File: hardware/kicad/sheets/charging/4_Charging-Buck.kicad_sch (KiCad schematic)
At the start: 38 parts, among them Q3 L2N7002SLLT1G, Q4 ME50P06-G, U7 68uF, U8 CN3722, U9 15uH

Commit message: various improvements
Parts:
- renumbered C5 to C12, C6 to C13, C7 to C14, C8 to C15, C9 to C16, C10 to C17, C11 to C18, C12 to C19, C13 to C20, C14 to C21, C15 to C22, C16 to C23, C17 to C24, D10 to D13, D11 to D14, R6 to R15, R7 to R16, R8 to R17, R9 to R18, R10 to R19, R11 to R20, R12 to R21, R13 to R22, R14 to R23, R15 to R24, R16 to R25, R17 to R26, R18 to R27, R19 to R28, R20 to R29, R21 to R30

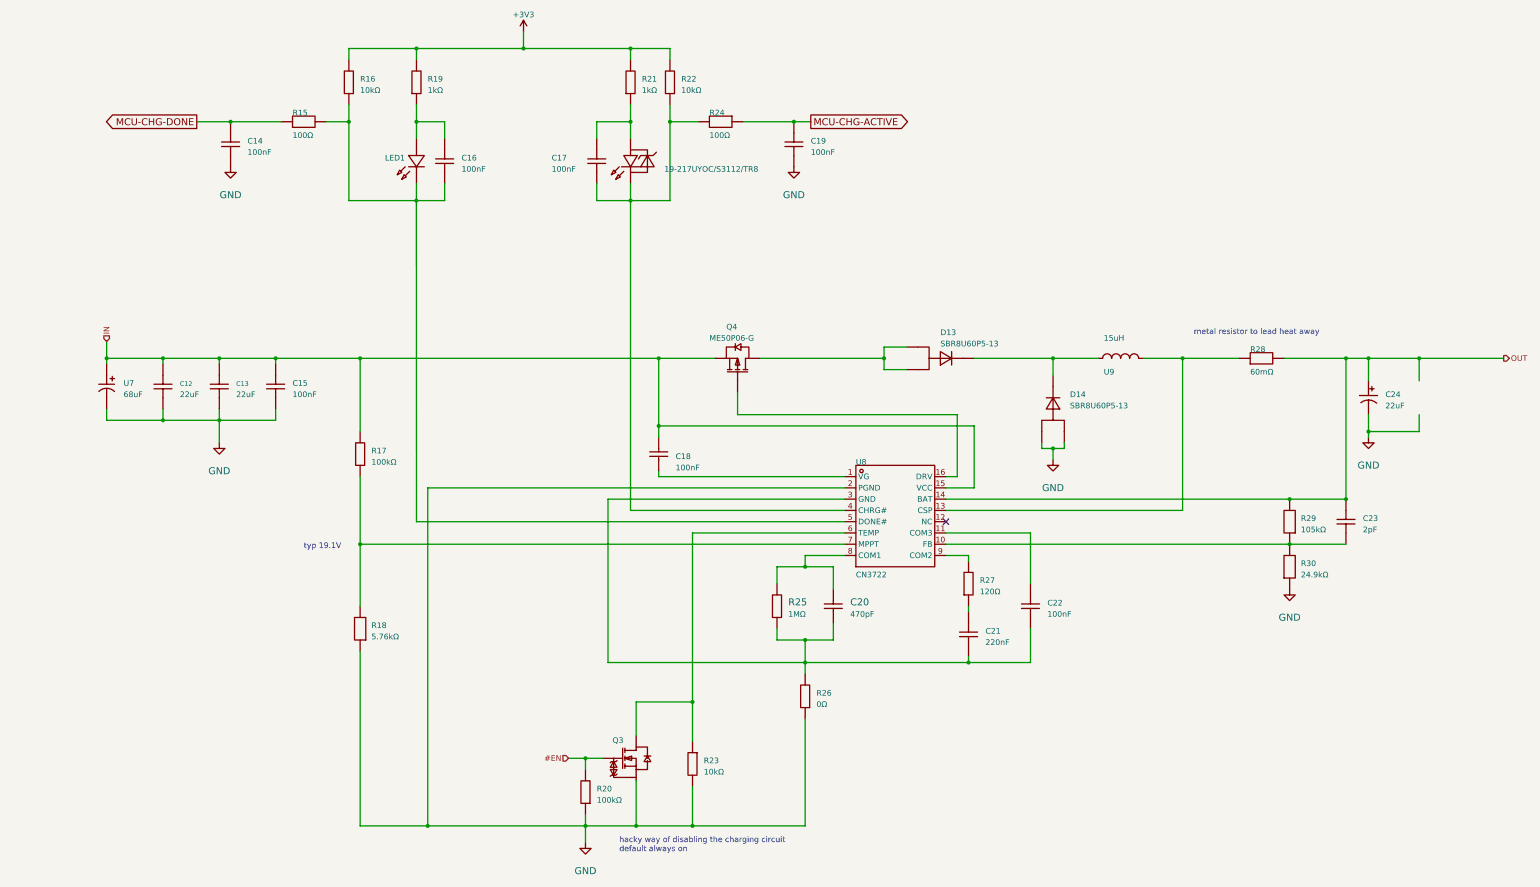
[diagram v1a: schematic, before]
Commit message: current sensing on the servos and cleaning up empty sheets
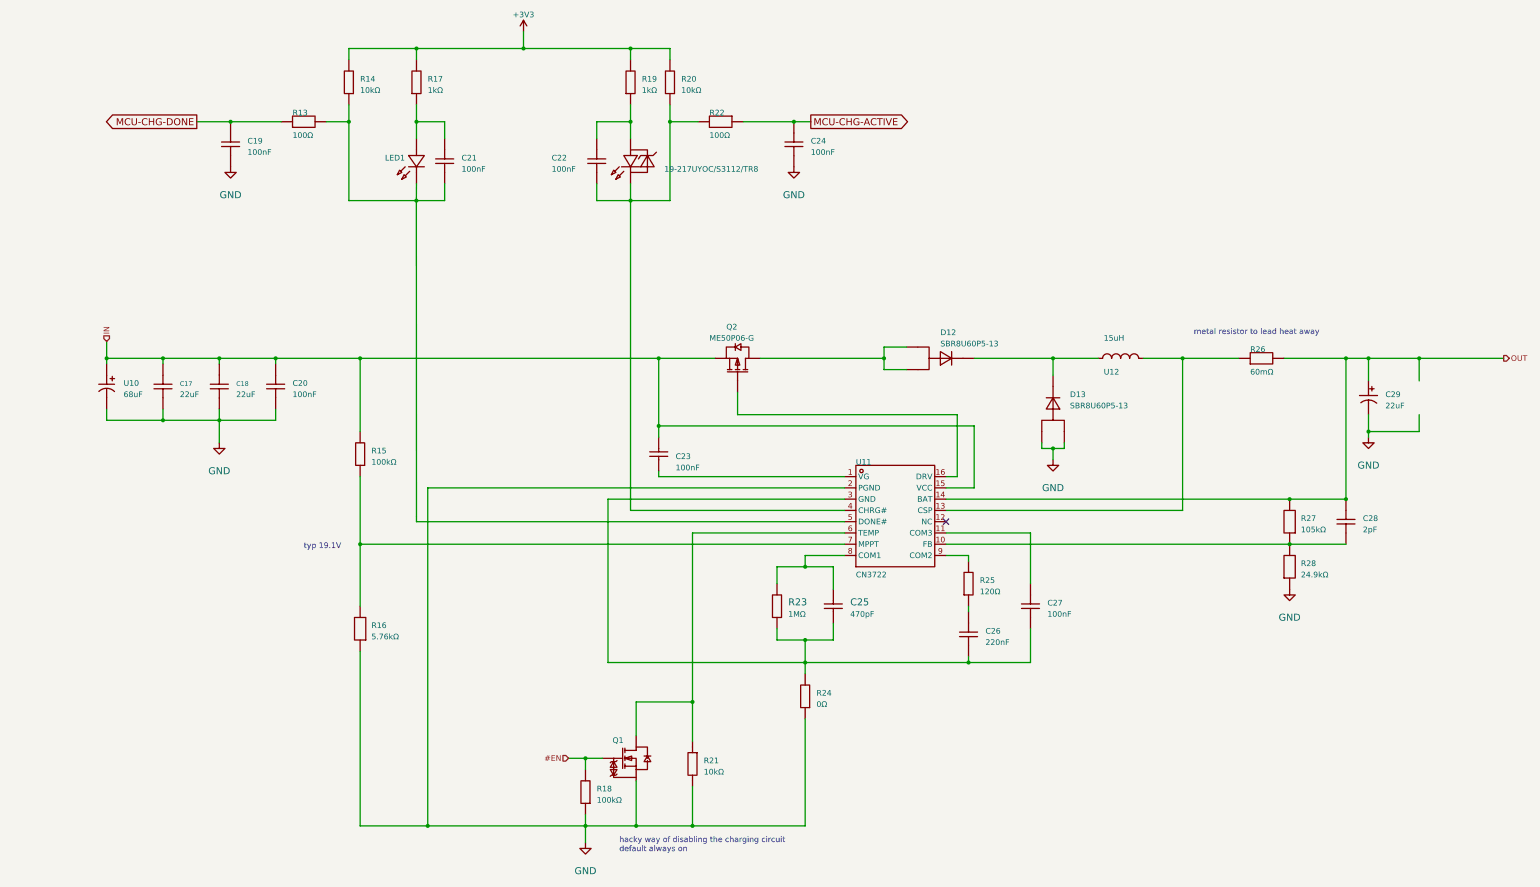
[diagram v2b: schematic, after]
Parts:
- renumbered C12 to C17, C13 to C18, C14 to C19, C15 to C20, C16 to C21, C17 to C22, C18 to C23, C19 to C24, C20 to C25, C21 to C26, C22 to C27, C23 to C28, C24 to C29, D13 to D12, D14 to D13, Q3 to Q1, Q4 to Q2, R15 to R13, R16 to R14, R17 to R15, R18 to R16, R19 to R17, R20 to R18, R21 to R19, R22 to R20, R23 to R21, R24 to R22, R25 to R23, R26 to R24, R27 to R25, R28 to R26, R29 to R27, R30 to R28, U7 to U10, U8 to U11, U9 to U12

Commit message: new references
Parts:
- renumbered C17 to C18, C18 to C19, C19 to C20, C20 to C21, C21 to C22, C22 to C23, C23 to C24, C24 to C25, C25 to C26, C26 to C27, C27 to C28, C28 to C29, C29 to C30, D12 to D11, D13 to D12, LED1 to LED6, LED2 to LED7, R13 to R35, R14 to R36, R15 to R37, R16 to R38, R17 to R39, R18 to R40, R19 to R41, R20 to R42, R21 to R43, R22 to R44, R23 to R45, R24 to R46, R25 to R47, R26 to R48, R27 to R49, R28 to R50, U10 to U15, U11 to U16, U12 to U17

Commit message: pre robot updating references
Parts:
- renumbered C18 to C17, C19 to C18, C20 to C19, C21 to C20, C22 to C21, C23 to C22, C24 to C23, C25 to C24, C26 to C25, C27 to C26, C28 to C27, C29 to C28, C30 to C29, R35 to R43, R36 to R44, R37 to R45, R38 to R46, R39 to R47, R40 to R48, R41 to R49, R42 to R50, R43 to R51, R44 to R52, R45 to R53, R46 to R54, R47 to R55, R48 to R56, R49 to R57, R50 to R58, U15 to U16, U16 to U17, U17 to U18

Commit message: various imprvements
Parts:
- added R196: --, symbol 5v rail sm-easyedapro:PE2512FKE7W0R06L
- renumbered C17 to C22, C18 to C23, C19 to C24, C20 to C25, C21 to C26, C22 to C27, C23 to C28, C24 to C29, C25 to C30, C26 to C31, C27 to C32, C28 to C33, C29 to C34, R43 to R73, R44 to R74, R45 to R75, R46 to R76, R47 to R77, R48 to R78, R49 to R79, R50 to R80, R51 to R81, R52 to R82, R53 to R83, R54 to R84, R55 to R85, R56 to R86, R57 to R87, R58 to R88, U16 to U22, U17 to U23, U18 to U24
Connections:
- net MCU-CHG-ACTIVE is gone; now on net Charger/CN3072/CHG-ACTIVE: C29.2, R82.1
- net MCU-CHG-DONE is gone; now on net Charger/CN3072/CHG-DONE: C24.2, R73.1
- net OUT: now also R196.2
- net at R86.1, U23.13 (CSP), U24.2: now also R196.1
- net Charger/CN3072/CHG-DONE: now reaches C27.1, LED7.1 (-), R80.1, R82.2, U23.4 (CHRG#)
- net Charger/CN3072/CHG-ACTIVE: now reaches C26.1, LED6.1 (K), R73.2, R74.1, U23.5 (DONE#)
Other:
- note added: "Default 3A, solder another in parallel for higher current"

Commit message: updated some footprints, fixed board
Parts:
- removed C34: 22uF, symbol 5v rail sm-easyedapro:RVT1H220M0605
- removed Q1: L2N7002SLLT1G, symbol 5v rail sm-easyedapro:L2N7002SLLT1G
- removed R73, R82: 100Ω, symbol 5v rail sm-easyedapro:FRC0402F1000TS
- removed R74, R80: 10kΩ, symbol 5v rail sm-easyedapro:0402WGF1002TCE
- removed U22: 68uF, symbol 5v rail sm-easyedapro:RVT1H680M0607
- added C135: RVT1H220M0605, JLCImport:RVT1H220M0605, symbol JLCImport:RVT1H220M0605
- added Q19: L2N7002SLLT1G, JLCImport:L2N7002SLLT1G, symbol JLCImport:L2N7002SLLT1G
- added R109, R73: 0603WAF1000T5E, JLCImport:0603WAF1000T5E, symbol JLCImport:0603WAF1000T5E
- added R74, R82: 10k, Resistor_SMD:R_0201_0603Metric, symbol Device:R
- added U69: RVT1H680M0607, JLCImport:RVT1H680M0607, symbol JLCImport:RVT1H680M0607
- C20: renamed from C22; footprint (none) -> 5v rail sm-easyedapro:C0805; now in the parts list
- C21: renamed from C23; footprint (none) -> 5v rail sm-easyedapro:C0805; now in the parts list
- C22: renamed from C24; footprint (none) -> 5v rail sm-easyedapro:C0402; now in the parts list
- C23: renamed from C25; footprint (none) -> 5v rail sm-easyedapro:C0402; now in the parts list
- C24: renamed from C26; footprint (none) -> 5v rail sm-easyedapro:C0402; now in the parts list
- C25: renamed from C27; footprint (none) -> 5v rail sm-easyedapro:C0402; now in the parts list
- C26: renamed from C28; footprint (none) -> 5v rail sm-easyedapro:C0402; now in the parts list
- C27: renamed from C29; footprint (none) -> 5v rail sm-easyedapro:C0402; now in the parts list
- C29: renamed from C31; footprint (none) -> 5v rail sm-easyedapro:C0603; now in the parts list
- C30: renamed from C32; footprint (none) -> 5v rail sm-easyedapro:C0402; now in the parts list
- C31: renamed from C33; footprint (none) -> 5v rail sm-easyedapro:C0402; now in the parts list
- D11: footprint (none) -> JLCImport:SBR8U60P5-13; now in the parts list
- D12: footprint 5v rail sm-easyedapro:POWERDI-5_L5.4-W4.0-LS6.5-RD -> JLCImport:SBR8U60P5-13
- LED6: footprint (none) -> JLCImport:PSC-1608U50GC-G4; Silkscreen (none) -> 100%; now in the parts list
- LED7: footprint (none) -> JLCImport:19-217UYOC_S3112_TR8; Silkscreen text (none) -> Charging; now in the parts list
- Q2: footprint (none) -> Package_TO_SOT_SMD:TO-252-2; now in the parts list
- R76, R77, R78, R81, R83, R85: footprint (none) -> Resistor_SMD:R_0603_1608Metric; now in the parts list
- R86: footprint (none) -> JLCImport:PE2512FKE7W0R06L; now in the parts list
- R87: renamed from R196; footprint (none) -> JLCImport:PE2512FKE7W0R06L; now not fitted
- R89: renamed from R88; footprint (none) -> Resistor_SMD:R_0603_1608Metric; now in the parts list
- U23: renamed from U24; now in the parts list
- renumbered C30 to C28, R87 to R88, U23 to U22
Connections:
- net #EN: now also Q19.1 (G)
- net +3V3: now also R74.1, R82.1
- net Charger/CN3072/CHG-ACTIVE: now also R109.2, R73.2, R74.2
- net Charger/CN3072/CHG-DONE: now also R109.1, R73.1, R82.2
- net GND: now also C135.2, Q19.2 (S)
- net OUT: now also C135.1
- net at R81.1, U22.6 (TEMP): now also Q19.3 (D)
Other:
- moved on the sheet: R78

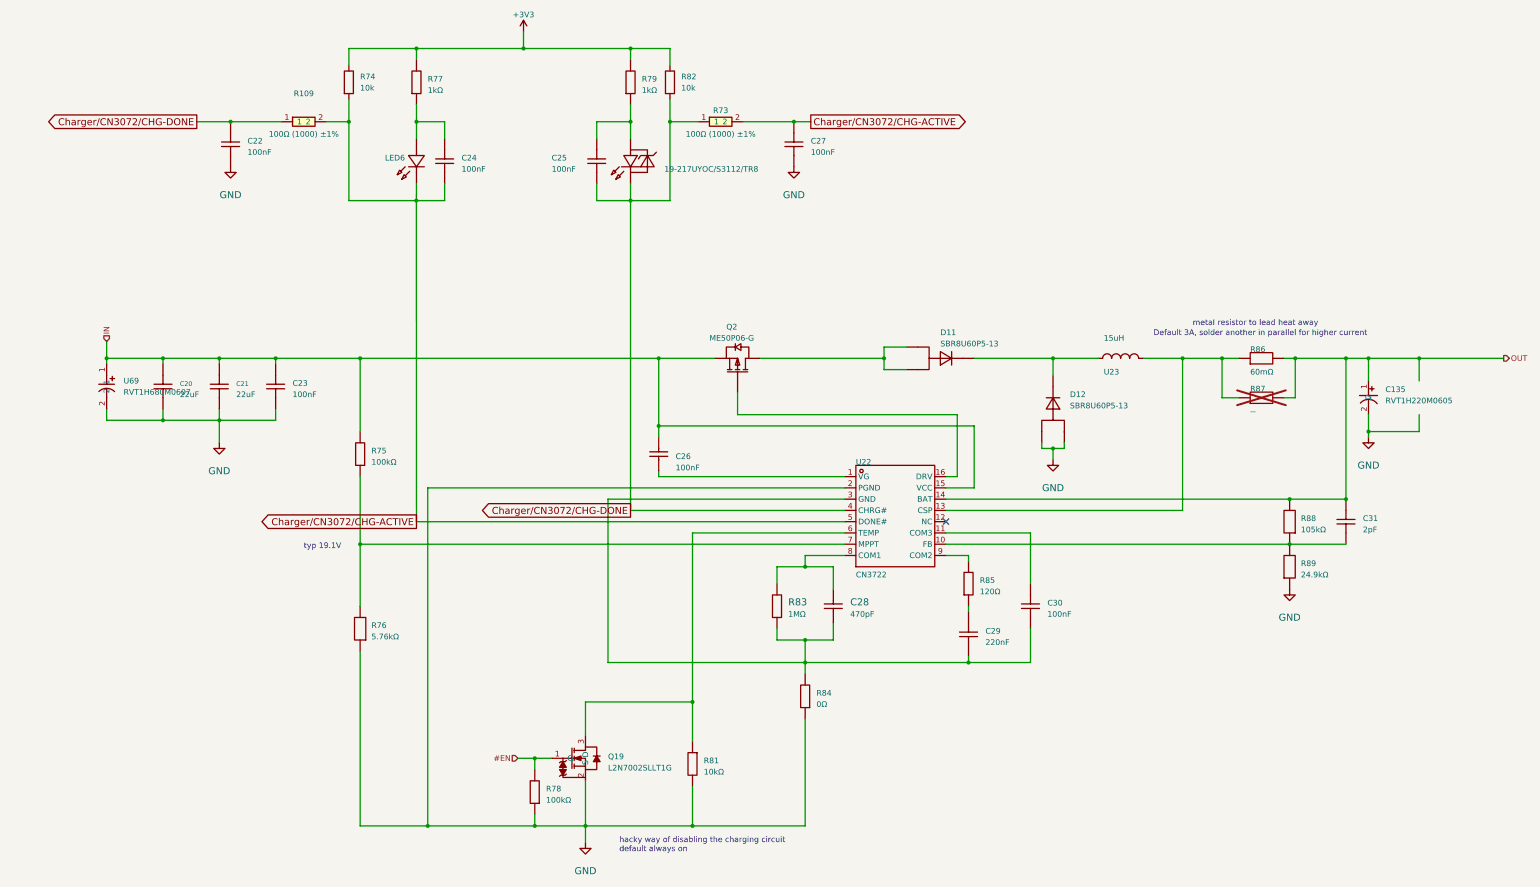
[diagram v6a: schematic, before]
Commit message: 5v usb c done, esc mostly done
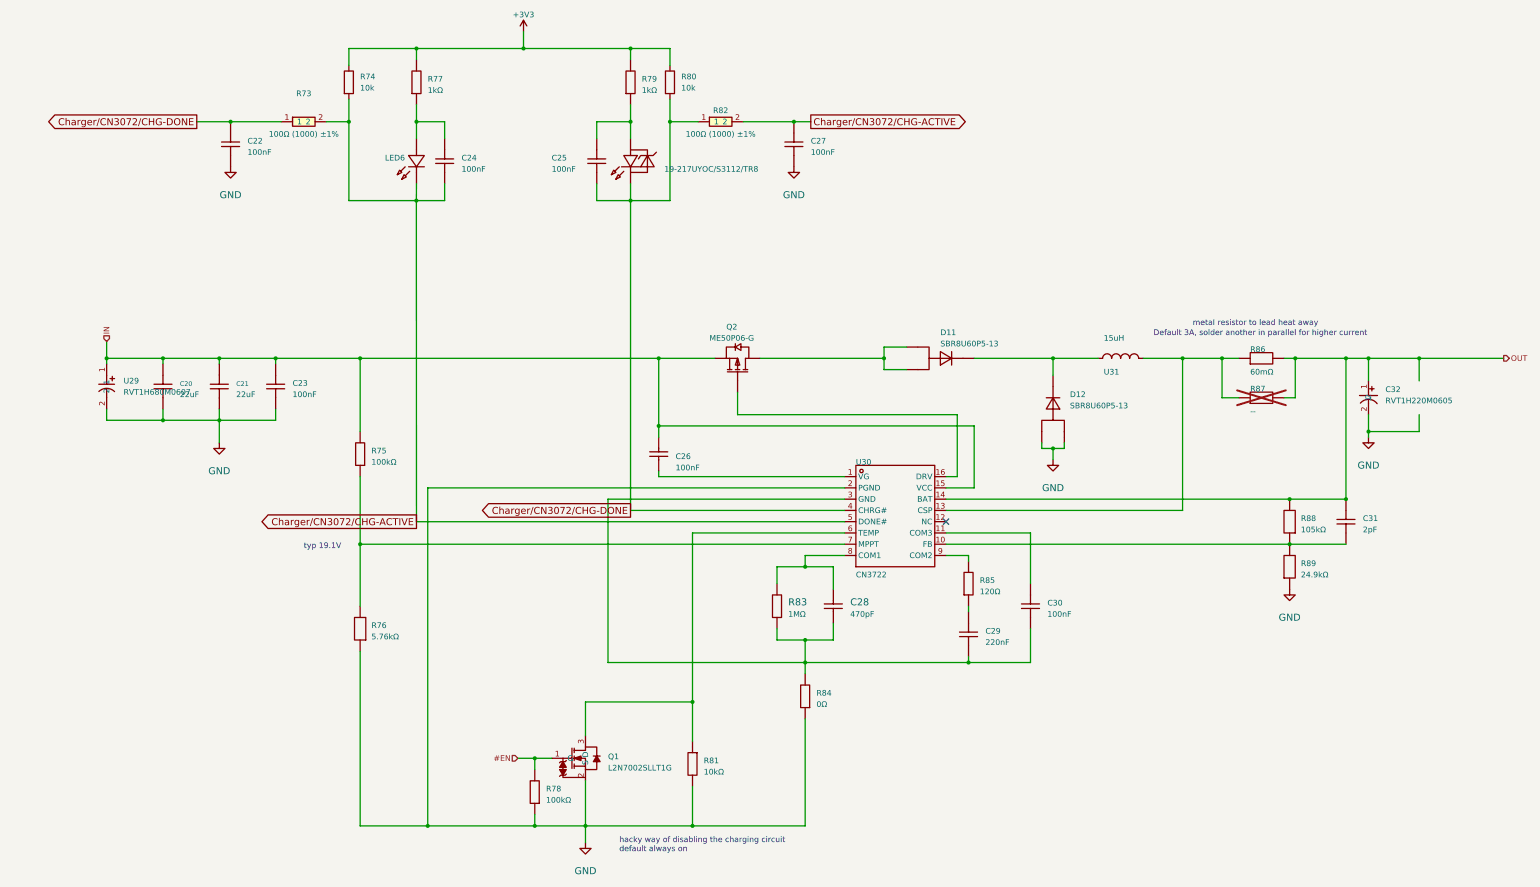
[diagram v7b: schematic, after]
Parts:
- renumbered C135 to C32, Q19 to Q1, R109 to R73, R82 to R80, R73 to R82, U69 to U29, U22 to U30, U23 to U31
